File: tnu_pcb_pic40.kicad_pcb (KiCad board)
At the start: 2 copper layers, 108 parts, among them CN1 USB_B_receptacle, J1 SCREWTERM, J2 JUMPER2, J3 JUMPER3, J4 JUMPER2, J5 PICKIT3, P1 TP, P10 TP, P11 TP, P12 TP, P13 TP, P14 TP, P15 TP, P16 TP, P17 TP, P18 TP, P19 TP, P2 TP, P3 TP, P4 TP, P5 TP, P6 TP, P7 TP, P8 TP, P9 TP, SW1 SW KEY-SPST, U1 FT231XS-R, U2 LD1117-3.3/SOT223, U3 PIC18F47Q84, U4 636L3C016M00000

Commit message: Board setup: outline, stackup, TNU design rules, Power net class
- Edge.Cuts rectangle (114.5, 60)-(180.7, 159): 66.2 x 99 mm.
- Stackup: 2-layer 1.6 mm FR4 (1.51 core), 1 oz copper, HAL SnPb finish.
- Rules: min clearance/track 0.178 mm, min via 0.45/0.3 mm (min annular
  ring 0.075 to match), Default class 0.254 mm track, 0.762/0.33 via.
- Power class 0.5 mm track: VCC, +3.3V, VCC5_USB, VCC_USB, Net-(J1-Pin_1).
No footprints moved or edited.
ERC 1 (unchanged). DRC 84 -> 4 + 152 unconnected + 24 parity: outline
error fixed; the 83 silk issues lie outside the new outline, where DRC
no longer checks them (hidden until parts are placed, not fixed).

Co-Authored-By: Claude Opus 5.5 <noreply@anthropic.com>
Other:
- board outline added: 66.2 x 99 mm
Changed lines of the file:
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@@
 	)
 	(setup
+		(stackup
+			(layer "F.SilkS"
+				(type "Top Silk Screen")
+			)
+			(layer "F.Paste"
+				(type "Top Solder Paste")
+			)
+			(layer "F.Mask"
+				(type "Top Solder Mask")
+				(thickness 0.01)
+			)
+			(layer "F.Cu"
+				(type "copper")
+				(thickness 0.035)
+			)
+			(layer "dielectric 1"
+				(type "core")
+				(thickness 1.51)
+				(material "FR4")
+				(epsilon_r 4.5)
+				(loss_tangent 0.02)
+			)
+			(layer "B.Cu"
+				(type "copper")
+				(thickness 0.035)
+			)
+			(layer "B.Mask"
+				(type "Bottom Solder Mask")
+				(thickness 0.01)
+			)
+			(layer "B.Paste"
+				(type "Bottom Solder Paste")
+			)
+			(layer "B.SilkS"
+				(type "Bottom Silk Screen")
+			)
+			(copper_finish "HAL SnPb")
+			(dielectric_constraints no)
+		)
 		(pad_to_mask_clearance 0)
 		(allow_soldermask_bridges_in_footprints no)
@@
 		)
 	)
+	(gr_rect
+		(start 114.5 60)
+		(end 180.7 159)
+		(stroke
+			(width 0.05)
+			(type default)
+		)
+		(fill no)
+		(layer "Edge.Cuts")
+	)
 	(embedded_fonts no)

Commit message: Add four provisional M3 plated mounting holes
MountingHole:MountingHole_3.2mm_M3_Pad (KiCad library; 3.2 mm plated,
6.4 mm pad, no net) as H1-H4 at (119.5, 65), (175.7, 65), (119.5, 154),
(175.7, 154): 5 mm in from the outline corners. Marked board_only so
schematic parity and Update PCB leave them alone. Provisional: to be
checked against the reference board photo.
ERC 1, DRC 4 + 152 unconnected + 24 parity (all unchanged).

Co-Authored-By: Claude Opus 5.5 <noreply@anthropic.com>
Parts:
- added H1: MountingHole_3.2mm_M3_Pad, MountingHole:MountingHole_3.2mm_M3_Pad, F.Cu at (119.5, 65.0)
- added H2: MountingHole_3.2mm_M3_Pad, MountingHole:MountingHole_3.2mm_M3_Pad, F.Cu at (175.7, 65.0)
- added H3: MountingHole_3.2mm_M3_Pad, MountingHole:MountingHole_3.2mm_M3_Pad, F.Cu at (119.5, 154.0)
- added H4: MountingHole_3.2mm_M3_Pad, MountingHole:MountingHole_3.2mm_M3_Pad, F.Cu at (175.7, 154.0)

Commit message: Update PCB from schematic; KiCad re-save of schematics
PCB: TP21 -> TP16 and TP44 -> TP18 renamed in place; new TP21 (GND)
added at (120.2, 140.1); pad nets updated on U3, C5, C6, J5, R7, SW1,
TP1, TP8, TP26, TP28, TP31, TP32. No footprint moved or removed.
KiCad added empty Datasheet/Description fields to H1-H4.
Schematics: KiCad re-save, item order only (no content change).
ERC 1 (U4 footprint filter). DRC 4 + 160 unconnected, parity 24 -> 0.

Co-Authored-By: Claude Opus 5.5 <noreply@anthropic.com>
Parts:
- added TP21: TP, TestPoint:TestPoint_Pad_D1.0mm, F.Cu at (120.2, 140.1)
- renumbered TP21 to TP16, TP44 to TP18
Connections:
- C5 pad 2: Net-(C5-Pad2) -> GND
- C6 pad 2: Net-(C5-Pad2) -> GND
- J5 pad 1: Net-(J5-Pin_1) -> /Microcontroller/MCLRn
- R7 pad 2: Net-(U3-~{MCLR}/VPP) -> /Microcontroller/MCLRn
- SW1 pad 1: Net-(J5-Pin_1) -> /Microcontroller/MCLRn
- TP1 pad 1: Net-(U3-~{MCLR}/VPP) -> /Microcontroller/MCLRn
- TP26 pad 1: /Microcontroller/USB_TXD -> /USB_TXD
- TP28 pad 1: /Microcontroller/USB_RXD -> /USB_RXD
- TP31 pad 1: Net-(U3-SCK/SCL/RC3) -> /Microcontroller/SCL
- TP32 pad 1: Net-(U3-SDI/SDA/RC4) -> /Microcontroller/SDA
- TP8 pad 1: Net-(U3-RB3/CCP2) -> /Microcontroller/RB3
- U3 pad 1: Net-(U3-~{MCLR}/VPP) -> /Microcontroller/MCLRn
- U3 pad 13: unconnected-(U3-OSC1/CLKIN-Pad13) -> /Microcontroller/CLK
- U3 pad 14: /Microcontroller/CLK -> unconnected-(U3-RA6/OSC2/CLKO-Pad14)
- U3 pad 18: Net-(U3-SCK/SCL/RC3) -> /Microcontroller/SCL
- U3 pad 23: Net-(U3-SDI/SDA/RC4) -> /Microcontroller/SDA
- U3 pad 25: /Microcontroller/USB_RXD -> /USB_RXD
- U3 pad 26: /Microcontroller/USB_TXD -> /USB_TXD
- U3 pad 36: Net-(U3-RB3/CCP2) -> /Microcontroller/RB3

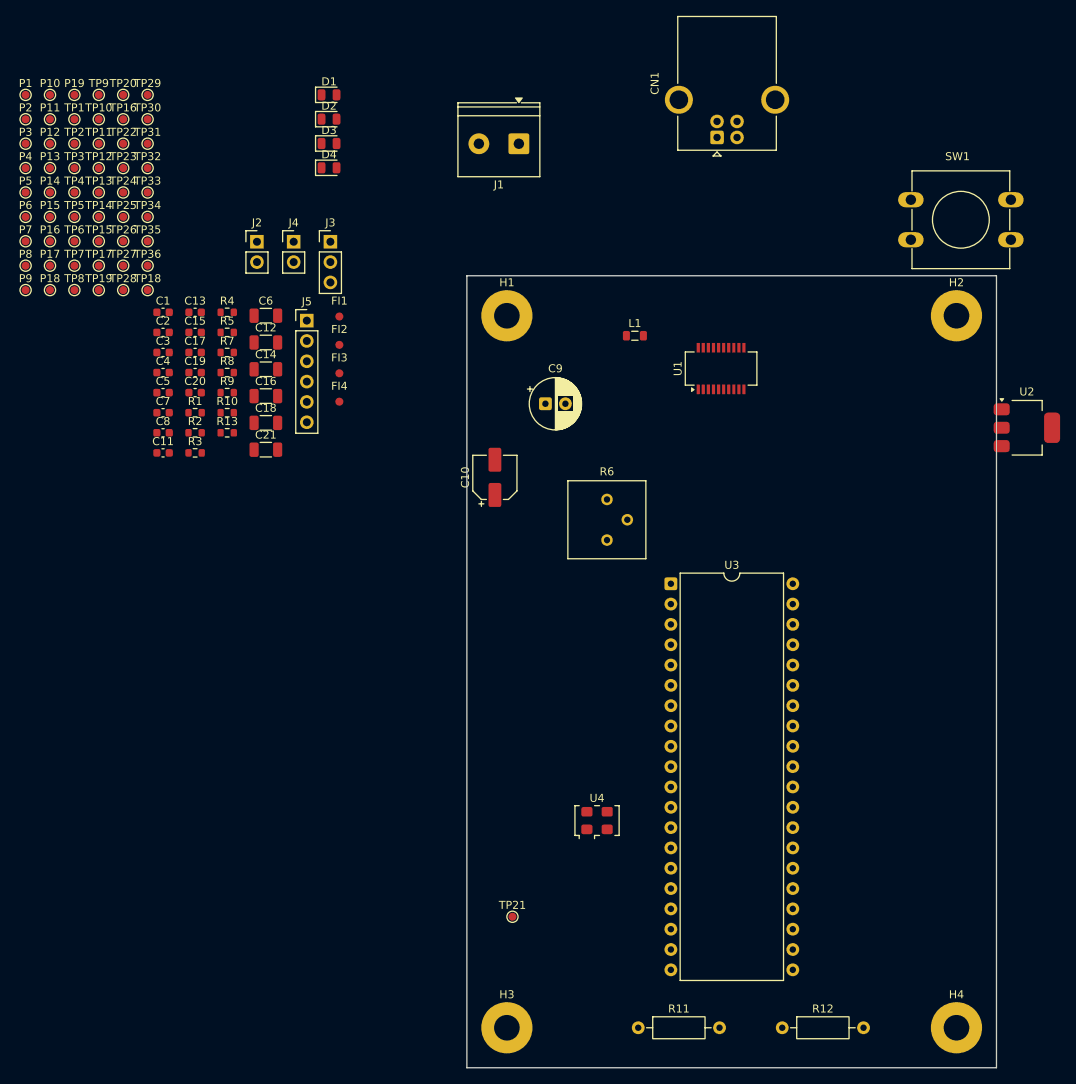
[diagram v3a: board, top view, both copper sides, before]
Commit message: Merge part placement from earlier layout
Source (read only): ..\TNU_PCB_Pic40\tnu_pcb_pic40\_restore_backup_2026-10-11T19-18-11-757\
_restore_backup_2026-10-15T03-24-19-758\tnu_pcb_pic40.kicad_pcb, matched by footprint UUID.
55 footprints placed: footprint (at) and Reference/Value (at) copied. For the 13 whose
rotation changes (C16-C21, R1, R2, R5, R7, R13, D1, D2), the angle was also copied onto
their pad/fp_text/property (at) lines (x, y unchanged); C16-C20, D1 and D2 also take the
source Reference position. All 230 matched pads verified identical in absolute position
and angle to the source. H1-H4 and the new TP21 untouched; no UUID added or removed.
ERC 1. DRC 35 + 160 unconnected, parity 0. Most DRC items are the provisional holes
H1-H4 colliding with FI1-FI4, J1, SW1 and R10 (holes not moved yet).

Co-Authored-By: Claude Opus 5.5 <noreply@anthropic.com>
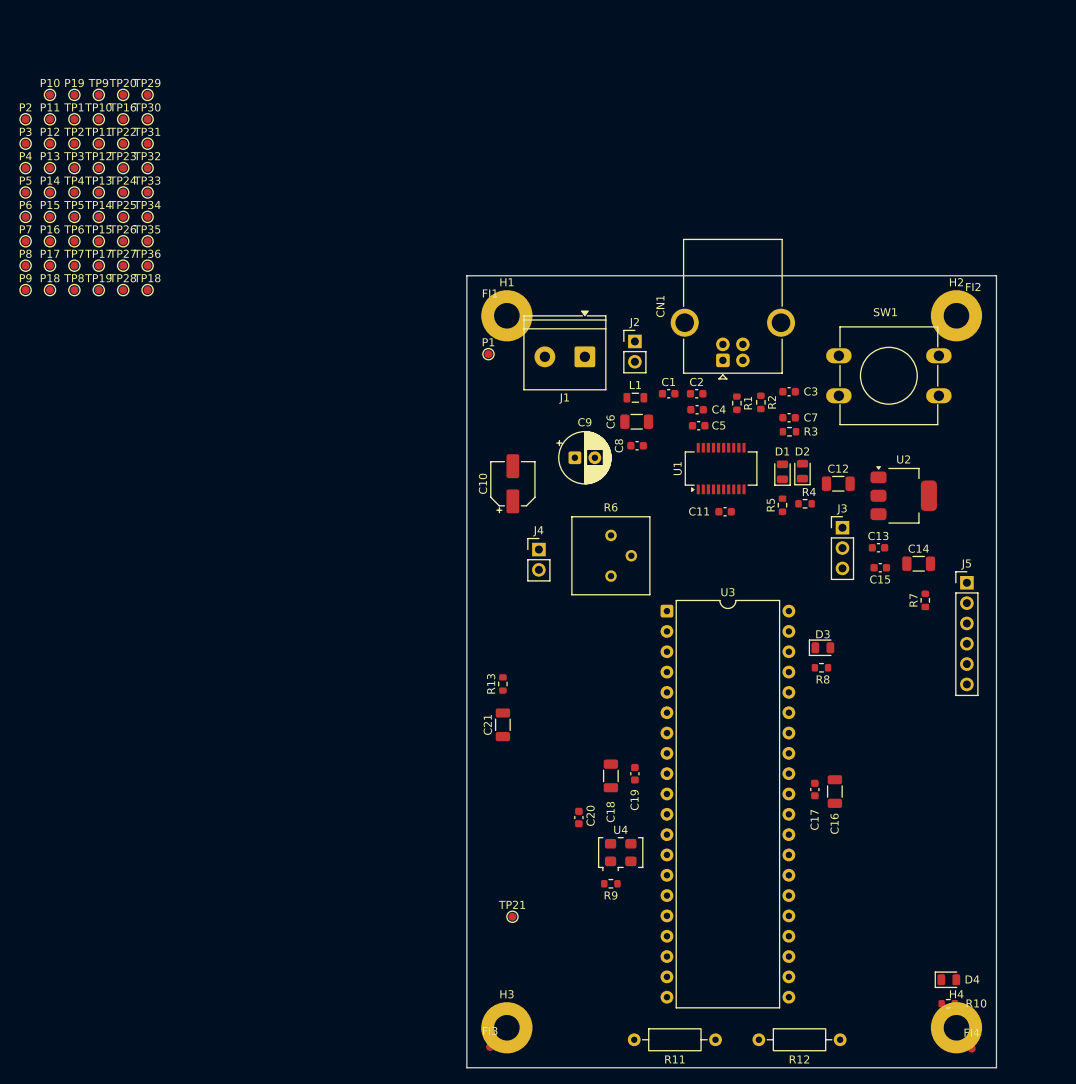
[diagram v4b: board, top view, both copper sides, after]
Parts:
- moved D4 127.7 mm to (174.7, 148.0)
- moved R10 116.5 mm to (174.7, 151.0)
- moved FI4 113.1 mm to (177.6, 156.6)
- moved C17 94.8 mm to (158.0, 124.2), turned to 90 degrees
- moved R7 92.6 mm to (171.8, 100.6), turned to 90 degrees
- moved C15 90.6 mm to (166.2, 96.5)
- moved C13 90.3 mm to (165.9, 94.0)
- moved J5 88.8 mm to (177.0, 98.4)
- moved D3 88.2 mm to (159.0, 106.5)
- moved C16 86.6 mm to (160.5, 124.5), turned to 90 degrees
- moved FI3 86.3 mm to (117.4, 156.4)
- moved C14 85.1 mm to (171.0, 96.0)
- moved R8 82.9 mm to (158.8, 109.0)
- moved FI2 79.4 mm to (177.8, 63.4)
- moved C3 78.4 mm to (154.8, 74.5)
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
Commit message: Place test point strips along U3
36 TP footprints moved (footprint (at) only; rotation 0, field offsets
unchanged). Signal TPs on U3 pin n: left strip x 124.27, y 101.92 +
2.54*(n-1) for n <= 20; right strip x 167.45, y 101.92 + 2.54*(40-n) for
n >= 21. Supply: TP19 VCC (124.27, 127.32), TP21 GND (124.27, 129.86),
TP16 VCC (167.45, 122.24), TP18 GND (167.45, 124.78). P2-P19 not moved.
ERC 1. DRC 82 + 160 unconnected, parity 0: the 47 new items are all
TP reference labels on the neighbouring TP's silkscreen/pad.

Co-Authored-By: Claude Opus 5.5 <noreply@anthropic.com>
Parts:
- moved TP30 138.0 mm to (167.4, 142.6)
- moved TP32 135.4 mm to (167.4, 145.1)
- moved TP34 132.8 mm to (167.4, 147.6)
- moved TP20 131.5 mm to (167.4, 127.3)
- moved TP36 130.3 mm to (167.4, 150.2)
- moved TP22 129.1 mm to (167.4, 129.9)
- moved TP23 128.7 mm to (167.4, 132.4)
- moved TP24 128.4 mm to (167.4, 134.9)
- moved TP16 126.1 mm to (167.4, 122.2)
- moved TP26 126.0 mm to (167.4, 137.5)
- moved TP28 123.8 mm to (167.4, 140.0)
- moved TP10 123.7 mm to (167.4, 114.6)
- moved TP12 121.6 mm to (167.4, 117.2)
- moved TP14 119.5 mm to (167.4, 119.7)
- moved TP4 117.1 mm to (167.4, 107.0)
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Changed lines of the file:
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@@
 	(footprint "TestPoint:TestPoint_Pad_D1.0mm"
 		(layer "F.Cu")
-		(at 71.54 40.44)
+		(at 167.45 122.24)
 		(descr "SMD pad as test Point, diameter 1.0mm")
 		(tags "test point SMD pad")
@@
 	(footprint "TestPoint:TestPoint_Pad_D1.0mm"
 		(layer "F.Cu")
-		(at 71.54 43.49)
+		(at 167.45 129.86)
 		(descr "SMD pad as test Point, diameter 1.0mm")
 		(tags "test point SMD pad")
@@
 	(footprint "TestPoint:TestPoint_Pad_D1.0mm"
 		(layer "F.Cu")
-		(at 74.59 61.79)
+		(at 167.45 124.78)
 		(descr "SMD pad as test Point, diameter 1.0mm")
 		(tags "test point SMD pad")
@@
 	(footprint "TestPoint:TestPoint_Pad_D1.0mm"
 		(layer "F.Cu")
-		(at 74.59 46.54)
+		(at 167.45 145.1)
 		(descr "SMD pad as test Point, diameter 1.0mm")
 		(tags "test point SMD pad")
@@
 	(footprint "TestPoint:TestPoint_Pad_D1.0mm"
 		(layer "F.Cu")
-		(at 68.49 46.54)
+		(at 167.45 117.16)
 		(descr "SMD pad as test Point, diameter 1.0mm")
 		(tags "test point SMD pad")
@@
 	(footprint "TestPoint:TestPoint_Pad_D1.0mm"
 		(layer "F.Cu")
-		(at 65.44 40.44)
+		(at 124.27 101.92)
 		(descr "SMD pad as test Point, diameter 1.0mm")
 		(tags "test point SMD pad")
@@
 	(footprint "TestPoint:TestPoint_Pad_D1.0mm"
 		(layer "F.Cu")
-		(at 120.198903 140.12465)
+		(at 124.27 129.86)
 		(descr "SMD pad as test Point, diameter 1.0mm")
 		(tags "test point SMD pad")
@@
 	(footprint "TestPoint:TestPoint_Pad_D1.0mm"
 		(layer "F.Cu")
-		(at 68.49 52.64)
+		(at 167.45 119.7)
 		(descr "SMD pad as test Point, diameter 1.0mm")
 		(tags "test point SMD pad")
@@
 	(footprint "TestPoint:TestPoint_Pad_D1.0mm"
 		(layer "F.Cu")
-		(at 74.59 37.39)
+		(at 124.27 142.56)
 		(descr "SMD pad as test Point, diameter 1.0mm")
 		(tags "test point SMD pad")
@@
 	(footprint "TestPoint:TestPoint_Pad_D1.0mm"
 		(layer "F.Cu")
-		(at 68.49 61.79)
+		(at 124.27 127.32)
 		(descr "SMD pad as test Point, diameter 1.0mm")
 		(tags "test point SMD pad")
@@
 	(footprint "TestPoint:TestPoint_Pad_D1.0mm"
 		(layer "F.Cu")
-		(at 68.49 58.74)
+		(at 124.27 124.78)
 		(descr "SMD pad as test Point, diameter 1.0mm")
 		(tags "test point SMD pad")
@@
 	(footprint "TestPoint:TestPoint_Pad_D1.0mm"
 		(layer "F.Cu")
-		(at 74.59 40.44)
+		(at 167.45 142.56)
 		(descr "SMD pad as test Point, diameter 1.0mm")
 		(tags "test point SMD pad")
@@
 	(footprint "TestPoint:TestPoint_Pad_D1.0mm"
 		(layer "F.Cu")
-		(at 68.49 49.59)
+		(at 124.27 119.7)
 		(descr "SMD pad as test Point, diameter 1.0mm")
 		(tags "test point SMD pad")
@@
 	(footprint "TestPoint:TestPoint_Pad_D1.0mm"
 		(layer "F.Cu")
-		(at 74.59 49.59)
+		(at 124.27 147.64)
 		(descr "SMD pad as test Point, diameter 1.0mm")
 		(tags "test point SMD pad")
@@
 	(footprint "TestPoint:TestPoint_Pad_D1.0mm"
 		(layer "F.Cu")
-		(at 65.44 46.54)
+		(at 124.27 107)
 		(descr "SMD pad as test Point, diameter 1.0mm")
 		(tags "test point SMD pad")
@@
 	(footprint "TestPoint:TestPoint_Pad_D1.0mm"
 		(layer "F.Cu")
-		(at 65.44 49.59)
+		(at 167.45 107)
 		(descr "SMD pad as test Point, diameter 1.0mm")
 		(tags "test point SMD pad")
@@
 	(footprint "TestPoint:TestPoint_Pad_D1.0mm"
 		(layer "F.Cu")
-		(at 71.54 37.39)
+		(at 167.45 127.32)
 		(descr "SMD pad as test Point, diameter 1.0mm")
 		(tags "test point SMD pad")
@@
 	(footprint "TestPoint:TestPoint_Pad_D1.0mm"
 		(layer "F.Cu")
-		(at 74.59 52.64)
+		(at 167.45 147.64)
 		(descr "SMD pad as test Point, diameter 1.0mm")
 		(tags "test point SMD pad")
@@
 	(footprint "TestPoint:TestPoint_Pad_D1.0mm"
 		(layer "F.Cu")
-		(at 71.54 49.59)
+		(at 167.45 134.94)
 		(descr "SMD pad as test Point, diameter 1.0mm")
 		(tags "test point SMD pad")
@@
 	(footprint "TestPoint:TestPoint_Pad_D1.0mm"
 		(layer "F.Cu")
-		(at 65.44 52.64)
+		(at 124.27 109.54)
 		(descr "SMD pad as test Point, diameter 1.0mm")
 		(tags "test point SMD pad")
@@
 	(footprint "TestPoint:TestPoint_Pad_D1.0mm"
 		(layer "F.Cu")
-		(at 71.54 61.79)
+		(at 167.45 140.02)
 		(descr "SMD pad as test Point, diameter 1.0mm")
 		(tags "test point SMD pad")
@@
 	(footprint "TestPoint:TestPoint_Pad_D1.0mm"
 		(layer "F.Cu")
-		(at 74.59 58.74)
+		(at 167.45 150.18)
 		(descr "SMD pad as test Point, diameter 1.0mm")
 		(tags "test point SMD pad")
@@
 	(footprint "TestPoint:TestPoint_Pad_D1.0mm"
 		(layer "F.Cu")
-		(at 71.54 46.54)
+		(at 167.45 132.4)
 		(descr "SMD pad as test Point, diameter 1.0mm")
 		(tags "test point SMD pad")
@@
 	(footprint "TestPoint:TestPoint_Pad_D1.0mm"
 		(layer "F.Cu")
-		(at 65.44 61.79)
+		(at 167.45 112.08)
 		(descr "SMD pad as test Point, diameter 1.0mm")
 		(tags "test point SMD pad")
@@
 	(footprint "TestPoint:TestPoint_Pad_D1.0mm"
 		(layer "F.Cu")
-		(at 71.54 55.69)
+		(at 167.45 137.48)
 		(descr "SMD pad as test Point, diameter 1.0mm")
 		(tags "test point SMD pad")
@@
 	(footprint "TestPoint:TestPoint_Pad_D1.0mm"
 		(layer "F.Cu")
-		(at 65.44 55.69)
+		(at 167.45 109.54)
 		(descr "SMD pad as test Point, diameter 1.0mm")
 		(tags "test point SMD pad")
@@
 	(footprint "TestPoint:TestPoint_Pad_D1.0mm"
 		(layer "F.Cu")
-		(at 74.59 55.69)
+		(at 124.27 150.18)
 		(descr "SMD pad as test Point, diameter 1.0mm")
 		(tags "test point SMD pad")
@@
 	(footprint "TestPoint:TestPoint_Pad_D1.0mm"
 		(layer "F.Cu")
-		(at 68.49 55.69)
+		(at 124.27 122.24)
 		(descr "SMD pad as test Point, diameter 1.0mm")
 		(tags "test point SMD pad")
@@
 	(footprint "TestPoint:TestPoint_Pad_D1.0mm"
 		(layer "F.Cu")
-		(at 74.59 43.49)
+		(at 124.27 145.1)
 		(descr "SMD pad as test Point, diameter 1.0mm")
 		(tags "test point SMD pad")
@@
 	(footprint "TestPoint:TestPoint_Pad_D1.0mm"
 		(layer "F.Cu")
-		(at 68.49 37.39)
+		(at 124.27 114.62)
 		(descr "SMD pad as test Point, diameter 1.0mm")
 		(tags "test point SMD pad")
@@
 	(footprint "TestPoint:TestPoint_Pad_D1.0mm"
 		(layer "F.Cu")
-		(at 71.54 52.64)
+		(at 124.27 137.48)
 		(descr "SMD pad as test Point, diameter 1.0mm")
 		(tags "test point SMD pad")
@@
 	(footprint "TestPoint:TestPoint_Pad_D1.0mm"
 		(layer "F.Cu")
-		(at 65.44 43.49)
+		(at 124.27 104.46)
 		(descr "SMD pad as test Point, diameter 1.0mm")
 		(tags "test point SMD pad")
@@
 	(footprint "TestPoint:TestPoint_Pad_D1.0mm"
 		(layer "F.Cu")
-		(at 68.49 40.44)
+		(at 167.45 114.62)
 		(descr "SMD pad as test Point, diameter 1.0mm")
 		(tags "test point SMD pad")
@@
 	(footprint "TestPoint:TestPoint_Pad_D1.0mm"
 		(layer "F.Cu")
-		(at 71.54 58.74)
+		(at 124.27 140.02)
 		(descr "SMD pad as test Point, diameter 1.0mm")
 		(tags "test point SMD pad")
@@
 	(footprint "TestPoint:TestPoint_Pad_D1.0mm"
 		(layer "F.Cu")
-		(at 68.49 43.49)
+		(at 124.27 117.16)
 		(descr "SMD pad as test Point, diameter 1.0mm")
 		(tags "test point SMD pad")
@@
 	(footprint "TestPoint:TestPoint_Pad_D1.0mm"
 		(layer "F.Cu")
-		(at 65.44 58.74)
+		(at 124.27 112.08)
 		(descr "SMD pad as test Point, diameter 1.0mm")
 		(tags "test point SMD pad")

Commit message: Swap test points to pin header footprint
Update PCB from Schematic (done in KiCad): the 55 TP/P footprints are now
tnu:TestPoint_PinHeader_1x01_P2.54mm. Verified against the previous commit:
113 footprints, no UUID removed or added, no position/rotation/layer/pad-net
change, H1-H4 unchanged, Edge.Cuts unchanged, nothing outside the footprints
changed. ERC 1 (U4). DRC 35 + 160 unconnected, parity 0 (the 47 TP label
silkscreen items are gone: the new footprint keeps its Reference on F.Fab).

Co-Authored-By: Claude Opus 5.5 <noreply@anthropic.com>
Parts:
- P1, P10, P11, P12, P13, P14, P15, P16, P17, P18, P19, P2, P3, P4, P5, P6, P7, P8, P9, TP1, TP10, TP11, TP12, TP13, TP14, TP15, TP16, TP17, TP18, TP19, TP2, TP20, TP21, TP22, TP23, TP24, TP25, TP26, TP27, TP28, TP29, TP3, TP30, TP31, TP32, TP33, TP34, TP35, TP36, TP4, TP5, TP6, TP7, TP8, TP9: footprint TestPoint:TestPoint_Pad_D1.0mm -> tnu:TestPoint_PinHeader_1x01_P2.54mm
